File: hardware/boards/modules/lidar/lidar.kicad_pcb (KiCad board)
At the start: 2 copper layers, 70.6 x 66 mm, 33 parts, among them J1 Conn_01x04_Socket, J2 Lidar, J3 Conn_01x03_Socket, J4 Conn_01x03_Socket, J5 Conn_01x03_Socket, J6 Conn_01x03_Socket, J7 Conn_01x05_Socket, J8 Conn_01x04_Socket, Q1 AO3401A, SW1 SW_Push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

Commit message: lidar PCB
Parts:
- removed G1: ~, Connector_PinHeader_2.54mm:PinHeader_1x05_P2.54mm_Vertical
- removed J7: Conn_01x05_Socket, Connector_PinHeader_2.54mm:PinHeader_1x05_P2.54mm_Vertical
- removed J8: Conn_01x04_Socket, Connector_PinHeader_2.54mm:PinHeader_1x04_P2.54mm_Vertical
- added C11: 12pF, Capacitor_SMD:C_0603_1608Metric_Pad1.08x0.95mm_HandSolder, F.Cu at (138.9, 105.7)
- added C12: 12pF, Capacitor_SMD:C_0603_1608Metric_Pad1.08x0.95mm_HandSolder, F.Cu at (138.9, 111.9)
- added C13: 100nF, Capacitor_SMD:C_0603_1608Metric_Pad1.08x0.95mm_HandSolder, F.Cu at (138.9, 113.7)
- added C14: 100nF, Capacitor_SMD:C_0603_1608Metric_Pad1.08x0.95mm_HandSolder, F.Cu at (141.6, 108.3)
- added C15: 1uF, Capacitor_SMD:C_0603_1608Metric_Pad1.08x0.95mm_HandSolder, F.Cu at (138.9, 115.9)
- C10: value 12pF -> 100nF
- C4: value 100nF -> 4.7uF
- C5: value 10uF -> 100nF; footprint Capacitor_THT:CP_Radial_D5.0mm_P2.00mm -> Capacitor_SMD:C_0603_1608Metric_Pad1.08x0.95mm_HandSolder
- C7, C8: value 0.1uF -> 100nF
- C9: value 12pF -> 10uF; footprint Capacitor_SMD:C_0603_1608Metric_Pad1.08x0.95mm_HandSolder -> Capacitor_SMD:CP_Elec_4x5.4
- D1: value LED -> GREEN
- D2: value LED -> RED
- J1: value Conn_01x04_Socket -> JST; footprint Connector_PinHeader_2.54mm:PinHeader_1x04_P2.54mm_Vertical -> Connector_JST:JST_XH_B5B-XH-A_1x05_P2.50mm_Vertical
- J2: value Lidar -> Dupont; footprint Connector_PinHeader_2.54mm:PinHeader_1x04_P2.54mm_Vertical -> Connector_PinHeader_2.54mm:PinHeader_1x06_P2.54mm_Vertical
- J3: value Conn_01x03_Socket -> Dupont; footprint Connector_PinHeader_2.54mm:PinHeader_1x03_P2.54mm_Vertical -> Connector_PinHeader_2.54mm:PinHeader_1x04_P2.54mm_Vertical
- J4: value Conn_01x03_Socket -> JST; footprint Connector_PinHeader_2.54mm:PinHeader_1x03_P2.54mm_Vertical -> Connector_JST:JST_XH_B4B-XH-A_1x04_P2.50mm_Vertical
- J5, J6: value Conn_01x03_Socket -> JST; footprint Connector_PinHeader_2.54mm:PinHeader_1x03_P2.54mm_Vertical -> Connector_JST:JST_XH_B3B-XH-A_1x03_P2.50mm_Vertical
- Q1: value AO3401A -> AO3400A; footprint Package_TO_SOT_SMD:SOT-23_Handsoldering -> Package_TO_SOT_SMD:SOT-23
- R4: value 10K -> 100
- R5: value 100 -> 10K
- U1: value ATmega128A-A -> ATmega128A
- Y1: value 8MHz -> 16MHz
- moved R6 44.1 mm to (131.6, 88.7), turned to 180 degrees
- moved J1 43.5 mm to (134.0, 92.6)
- moved J5 40.0 mm to (125.8, 113.7), turned to 90 degrees
- moved J6 38.1 mm to (133.0, 113.7), turned to 90 degrees
- moved R5 35.3 mm to (135.9, 86.0), turned to -90 degrees
- moved R4 34.6 mm to (135.2, 88.7), turned to 180 degrees
- moved Q1 34.5 mm to (132.7, 86.0)
- moved C4 33.1 mm to (141.6, 91.2), turned to -90 degrees
- moved J2 29.6 mm to (142.5, 87.5), turned to 90 degrees
- moved R3 27.9 mm to (157.7, 114.6), turned to -90 degrees
- moved C1 26.7 mm to (138.9, 96.3), turned to 0 degrees
- moved C9 24.5 mm to (126.7, 87.7), turned to 135 degrees
- moved D2 24.2 mm to (157.7, 110.8), turned to 90 degrees
- moved R2 23.8 mm to (155.8, 114.6), turned to -90 degrees
- moved C10 22.5 mm to (124.6, 90.4), turned to 135 degrees
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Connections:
- C1 pad 2: Net-(C1-Pad2) -> GND
- C10 pad 1: Net-(U2-XIN32) -> 5V
- C10 pad 2: GND -> Net-(J4-Pin_3)
- C4 pad 2: Net-(U1-AREF) -> GND
- C5 pad 1: Net-(J2-Pin_1) -> 3V3
- C6 pad 1: Net-(J2-Pin_1) -> 3V3
- C7 pad 1: Net-(U2-CAP) -> 3V3
- C8 pad 1: GND -> 3V3
- C8 pad 2: 3V3 -> Net-(U1-AREF)
- C9 pad 1: Net-(U2-XOUT32) -> 5V
- C9 pad 2: GND -> Net-(J4-Pin_3)
- J1 pad 1: RX0 -> 3V3
- J1 pad 2: TX0 -> 5V
- J1 pad 3: 3V3 -> GND
- J1 pad 4: GND -> SDA
- J2 pad 1: Net-(J2-Pin_1) -> SCK
- J2 pad 2: Net-(J2-Pin_2) -> TX0
- J2 pad 3: GND -> RX0
- J2 pad 4: LIDAR_PWM -> RST
- J3 pad 1: ADC0 -> TX0
- J3 pad 2: ADC1 -> RX0
- J3 pad 3: ADC2 -> 3V3
- J4 pad 1: GND -> 5V
- J4 pad 2: 5V -> Net-(J4-Pin_2)
- J4 pad 3: SERVO_A_PWM -> Net-(J4-Pin_3)
- J5 pad 3: SERVO_B_PWM -> SERVO_A_PWM
- J6 pad 3: SERVO_C_PWM -> SERVO_B_PWM
- Q1 pad 1: GND -> Net-(Q1-G)
- Q1 pad 2: 5V -> GND
- Q1 pad 3: Net-(J2-Pin_1) -> Net-(J4-Pin_3)
- R4 pad 1: GND -> LIDAR_EN
- R4 pad 2: 5V -> Net-(Q1-G)
- R5 pad 1: LIDAR_EN -> GND
- R5 pad 2: GND -> Net-(Q1-G)
- R6 pad 2: Net-(J2-Pin_2) -> Net-(J4-Pin_2)
- SW1 pad 1: Net-(C1-Pad2) -> GND
- U1 pad 10: DEBUG_0 -> unconnected-(U1-PB0-Pad10)
- U1 pad 11: DEBUG_1 -> SCK
- U1 pad 12: DEBUG_2 -> unconnected-(U1-PB2-Pad12)
- U1 pad 13: DEBUG_3 -> unconnected-(U1-PB3-Pad13)
- U1 pad 14: DEBUG_4 -> unconnected-(U1-PB4-Pad14)
- U1 pad 15: LIDAR_PWM -> SERVO_A_PWM
- U1 pad 16: LIDAR_EN -> SERVO_B_PWM
- U1 pad 5: SERVO_A_PWM -> LIDAR_PWM
- U1 pad 59: ADC2 -> unconnected-(U1-PF2-Pad59)
- U1 pad 6: SERVO_B_PWM -> LIDAR_EN
- U1 pad 60: ADC1 -> unconnected-(U1-PF1-Pad60)
- U1 pad 61: ADC0 -> unconnected-(U1-PF0-Pad61)
- U1 pad 7: SERVO_C_PWM -> unconnected-(U1-PE5-Pad7)
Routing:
- net SERVO_C_PWM: track 51.3 -> 0.00 mm, vias 2 -> 0
- net DEBUG_0: track 34.3 -> 0.00 mm
- net RST: track 7.86 -> 41.8 mm, vias 0 -> 4
- net SERVO_B_PWM: track 41.6 -> 10.2 mm
- net DEBUG_1: track 30.7 -> 0.00 mm
- net RX0: track 61.6 -> 32.3 mm, vias 0 -> 2
- net TX0: track 46.3 -> 18.3 mm, vias 0 -> 4
- net DEBUG_2: track 27.0 -> 0.00 mm
- net 5V: track 69.5 -> 44.7 mm, vias 1 -> 0
- net RX1: track 30.9 -> 6.95 mm, vias 0 -> 2
- net DEBUG_3: track 23.4 -> 0.00 mm
- net Net-(J4-Pin_3): track 0.00 -> 21.5 mm
- net SCK: track 0.00 -> 21.5 mm, vias 0 -> 2
- net DEBUG_4: track 20.1 -> 0.00 mm
- net LIDAR_PWM: track 40.0 -> 20.7 mm, vias 0 -> 4
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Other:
- board size 70.6 x 66 mm -> 40 x 37 mm
- board text added: "2026 FB"
- board text added: "40x37mm"
- board text added: "A"
- board text added: "B"
- board text added: "I2C"
- board text added: "ISP"
- board text added: "LIDAR"
- board text added: "SERVOS"
- board text added: "UART"
- board text added: "VEMAR - LIDAR"

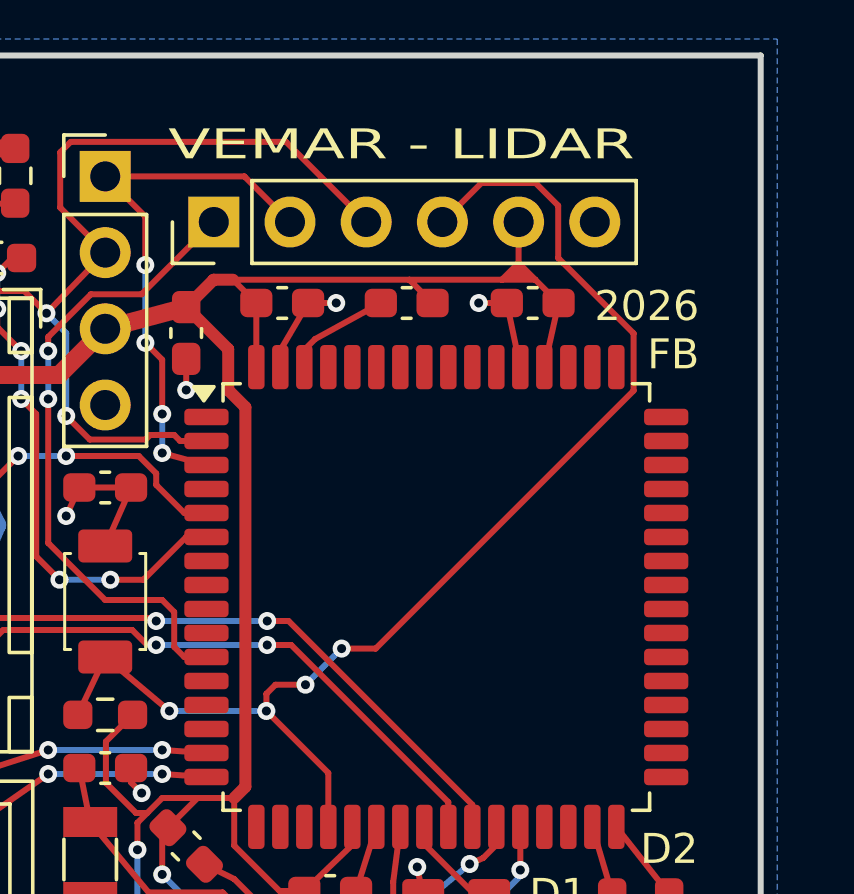
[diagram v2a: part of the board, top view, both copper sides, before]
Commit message: added teardrops to lidar and car PCB, should be good
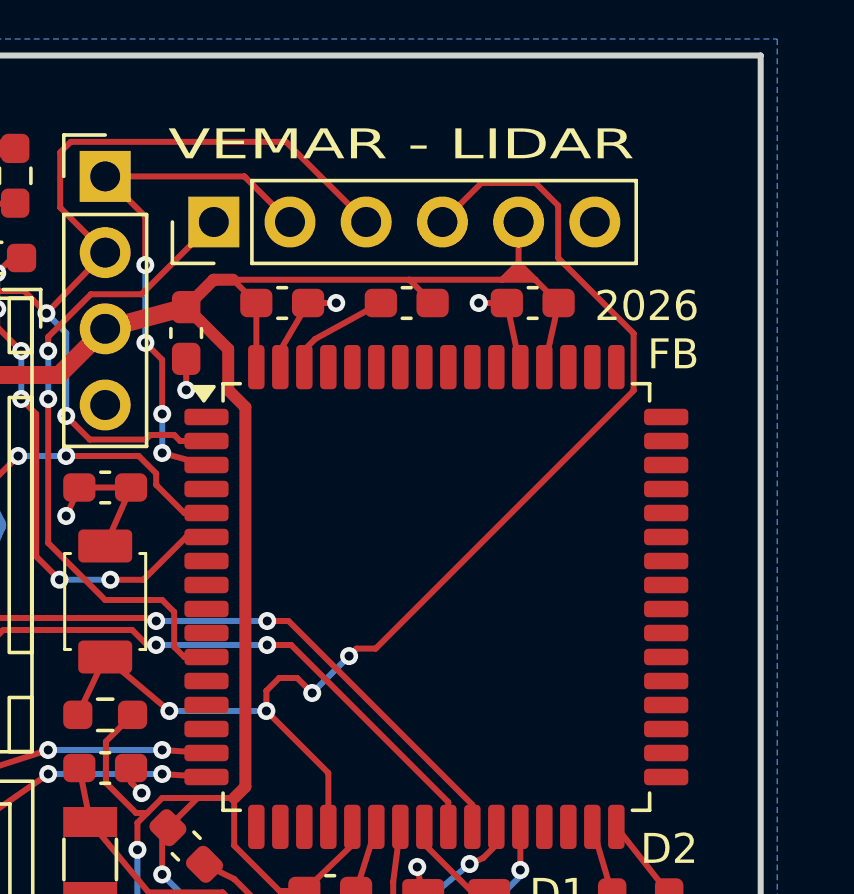
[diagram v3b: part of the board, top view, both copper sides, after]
